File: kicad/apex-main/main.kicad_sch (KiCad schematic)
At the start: 13 parts, among them J1 Conn_01x14, J2 Conn_01x14_Socket, J4 Conn_01x03_Socket, J5 Conn_01x06, J6 Conn_01x08, J7 Conn_01x07, J8 Conn_01x09

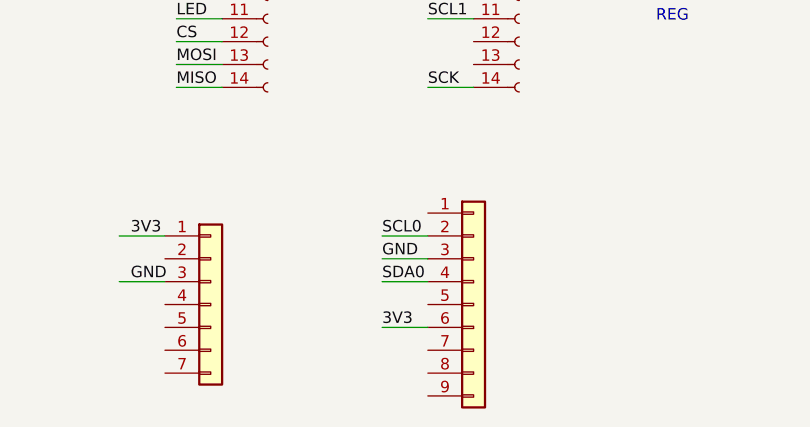
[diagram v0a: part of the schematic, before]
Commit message: Cleaned up BMI088 pinout
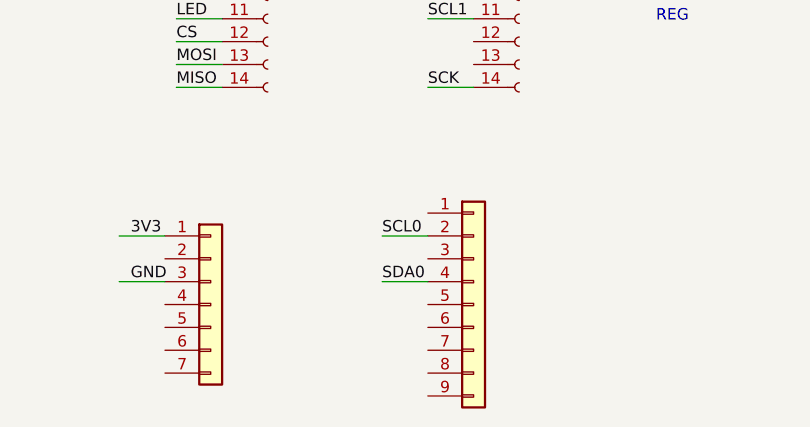
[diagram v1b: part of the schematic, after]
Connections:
- net 3V3: no longer J8.6 (Pin_6)
- net GND: no longer J8.3 (Pin_3)
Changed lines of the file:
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@@
-	(wire
-		(pts
-			(xy 114.3 158.75) (xy 119.38 158.75)
-		)
-		(stroke
-			(width 0)
-			(type default)
-		)
-	)
 	(wire
 		(pts
@@
 		(pts
 			(xy 50.8 135.89) (xy 54.61 135.89)
-		)
-		(stroke
-			(width 0)
-			(type default)
-		)
-	)
-	(wire
-		(pts
-			(xy 114.3 151.13) (xy 119.38 151.13)
 		)
 		(stroke
@@
 		)
 	)
-	(label "GND"
-		(at 114.3 151.13 0)
-		(effects
-			(font
-				(size 1.27 1.27)
-			)
-			(justify left bottom)
-		)
-	)
 	(label "SCL0"
 		(at 119.38 116.84 0)
@@
 		(effects
 			(font
-				(size 1.27 1.27)
-			)
-			(justify left bottom)
-		)
-	)
-	(label "3V3"
-		(at 114.3 158.75 0)
-		(effects
-			(font
